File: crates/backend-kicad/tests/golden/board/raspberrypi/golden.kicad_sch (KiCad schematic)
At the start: 1 part, among them U1 U

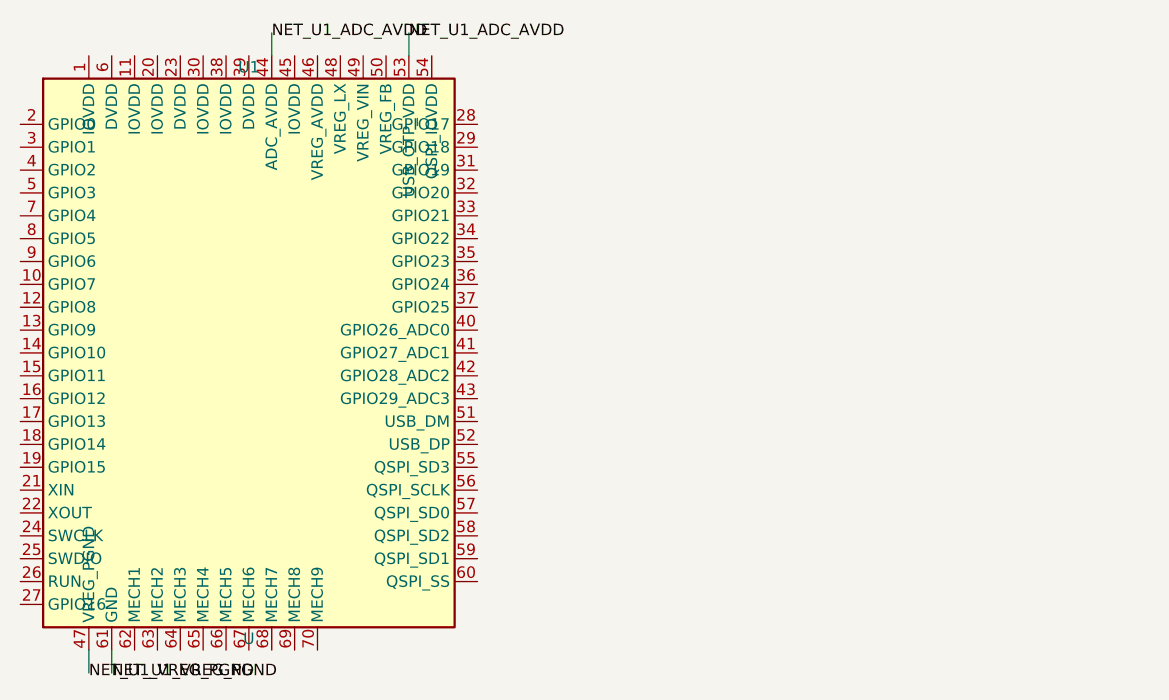
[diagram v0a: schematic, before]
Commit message: Improve recognition of bypass caps
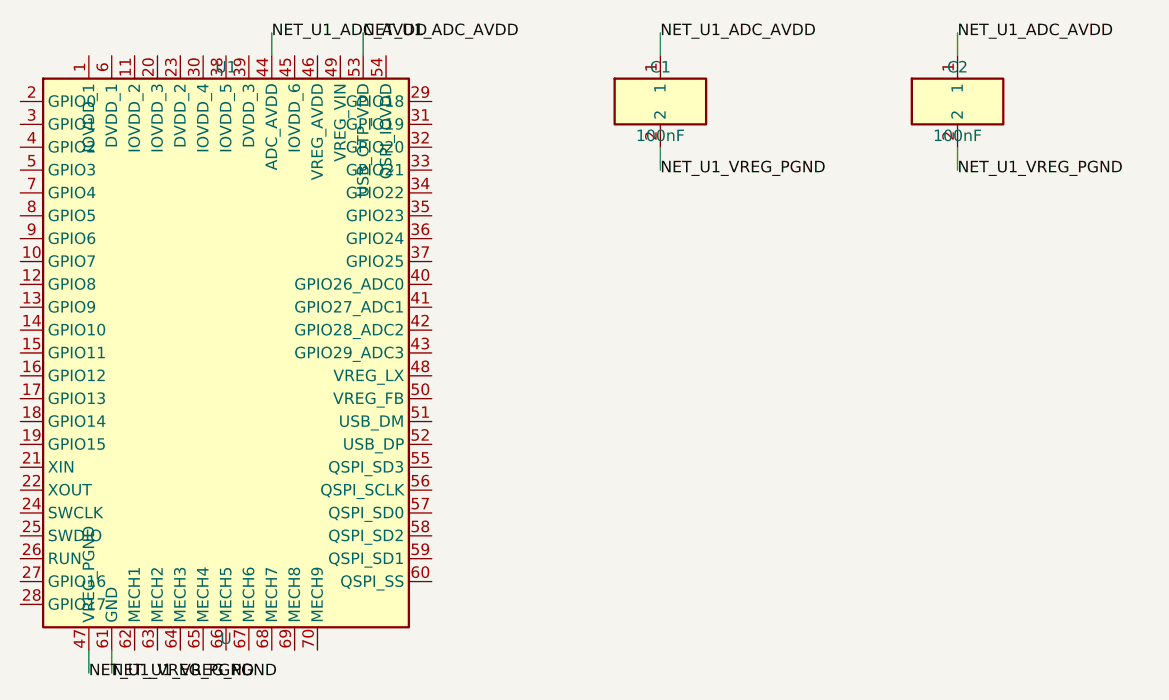
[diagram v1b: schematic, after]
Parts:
- added C1, C2: 100nF, Capacitor_SMD.3dshapes/C_0603_1608Metric, symbol copperleaf:Capacitor
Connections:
- net NET_U1_ADC_AVDD: now also C1.1, C2.1
- net NET_U1_VREG_PGND: now also C1.2, C2.2
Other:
- moved on the sheet: U1
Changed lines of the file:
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@@
   (symbol
     (lib_id "copperleaf:RP2354A")
-    (at 53.34 60.96 0)
+    (at 50.8 60.96 0)
     (unit 1)
     (in_bom yes)
@@
     (dnp no)
     (property "Reference" "U1"
-      (at 53.34 29.21 0)
+      (at 50.8 29.21 0)
       (effects
         (font
           (size 1.27 1.27))))
     (property "Value" "U"
-      (at 53.34 92.71 0)
+      (at 50.8 92.71 0)
       (effects
         (font
           (size 1.27 1.27))))
     (property "Footprint" "RP2354A"
-      (at 53.34 60.96 0)
+      (at 50.8 60.96 0)
       (hide yes)
       (effects
@@
         (path "/ c03958cf-0c1f-5189-d806-14e000c8b373"
           (reference "U1")
+          (unit 1)))))
+  (symbol
+    (lib_id "copperleaf:Capacitor")
+    (at 99.06 33.02 0)
+    (unit 1)
+    (in_bom yes)
+    (on_board yes)
+    (dnp no)
+    (property "Reference" "C1"
+      (at 99.06 29.21 0)
+      (effects
+        (font
+          (size 1.27 1.27))))
+    (property "Value" "100nF"
+      (at 99.06 36.83 0)
+      (effects
+        (font
+          (size 1.27 1.27))))
+    (property "Footprint" "Capacitor_SMD.3dshapes/C_0603_1608Metric"
+      (at 99.06 33.02 0)
+      (hide yes)
+      (effects
+        (font
+          (size 1.27 1.27))))
+    (property "Bypass" "yes"
+      (at 99.06 33.02 0)
+      (hide yes)
+      (effects
+        (font
+          (size 1.27 1.27))))
+    (instances
+      (project ""
+        (path "/ c03958cf-0c1f-5189-d806-14e000c8b373"
+          (reference "C1")
+          (unit 1)))))
+  (symbol
+    (lib_id "copperleaf:Capacitor")
+    (at 132.08 33.02 0)
+    (unit 1)
+    (in_bom yes)
+    (on_board yes)
+    (dnp no)
+    (property "Reference" "C2"
+      (at 132.08 29.21 0)
+      (effects
+        (font
+          (size 1.27 1.27))))
+    (property "Value" "100nF"
+      (at 132.08 36.83 0)
+      (effects
+        (font
+          (size 1.27 1.27))))
+    (property "Footprint" "Capacitor_SMD.3dshapes/C_0603_1608Metric"
+      (at 132.08 33.02 0)
+      (hide yes)
+      (effects
+        (font
+          (size 1.27 1.27))))
+    (property "Bypass" "yes"
+      (at 132.08 33.02 0)
+      (hide yes)
+      (effects
+        (font
+          (size 1.27 1.27))))
+    (instances
+      (project ""
+        (path "/ c03958cf-0c1f-5189-d806-14e000c8b373"
+          (reference "C2")
           (unit 1)))))
   (wire
@@
   (wire
     (pts
-      (xy 71.12 27.94)
-      (xy 71.12 25.4))
+      (xy 66.04 27.94)
+      (xy 66.04 25.4))
     (stroke
       (width 0))
 )
   (label "NET_U1_ADC_AVDD"
-    (at 71.12 25.4 0)
+    (at 66.04 25.4 0)
+    (effects
+      (font
+        (size 1.27 1.27)))
+)
+  (wire
+    (pts
+      (xy 99.06 27.94)
+      (xy 99.06 25.4))
+    (stroke
+      (width 0))
+)
+  (label "NET_U1_ADC_AVDD"
+    (at 99.06 25.4 0)
+    (effects
+      (font
+        (size 1.27 1.27)))
+)
+  (wire
+    (pts
+      (xy 132.08 27.94)
+      (xy 132.08 25.4))
+    (stroke
+      (width 0))
+)
+  (label "NET_U1_ADC_AVDD"
+    (at 132.08 25.4 0)
     (effects
       (font
@@
     (effects
       (font
+        (size 1.27 1.27)))
+)
+  (wire
+    (pts
+      (xy 99.06 38.1)
+      (xy 99.06 40.64))
+    (stroke
+      (width 0))
+)
+  (label "NET_U1_VREG_PGND"
+    (at 99.06 40.64 0)
+    (effects
+      (font
+        (size 1.27 1.27)))
+)
+  (wire
+    (pts
+      (xy 132.08 38.1)
+      (xy 132.08 40.64))
+    (stroke
+      (width 0))
+)
+  (label "NET_U1_VREG_PGND"
+    (at 132.08 40.64 0)
+    (effects
+      (font

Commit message: Apply stabilise-copperleaf-pipeline
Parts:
- C1, C2: footprint Capacitor_SMD.3dshapes/C_0603_1608Metric -> Capacitor_SMD:C_0603_1608Metric
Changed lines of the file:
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@@
         (font
           (size 1.27 1.27))))
-    (property "Footprint" "Capacitor_SMD.3dshapes/C_0603_1608Metric"
+    (property "Footprint" "Capacitor_SMD:C_0603_1608Metric"
       (at 99.06 33.02 0)
       (hide yes)
@@
         (font
           (size 1.27 1.27))))
-    (property "Footprint" "Capacitor_SMD.3dshapes/C_0603_1608Metric"
+    (property "Footprint" "Capacitor_SMD:C_0603_1608Metric"
       (at 132.08 33.02 0)
       (hide yes)
